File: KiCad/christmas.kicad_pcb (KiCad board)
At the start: 2 copper layers, 81.3 x 81.3 mm, 38 parts, among them J1 Conn_01x04, J2 Conn_01x04, J3 Batery_9V, U1 NE555P, U2 4015, U3 NE555P

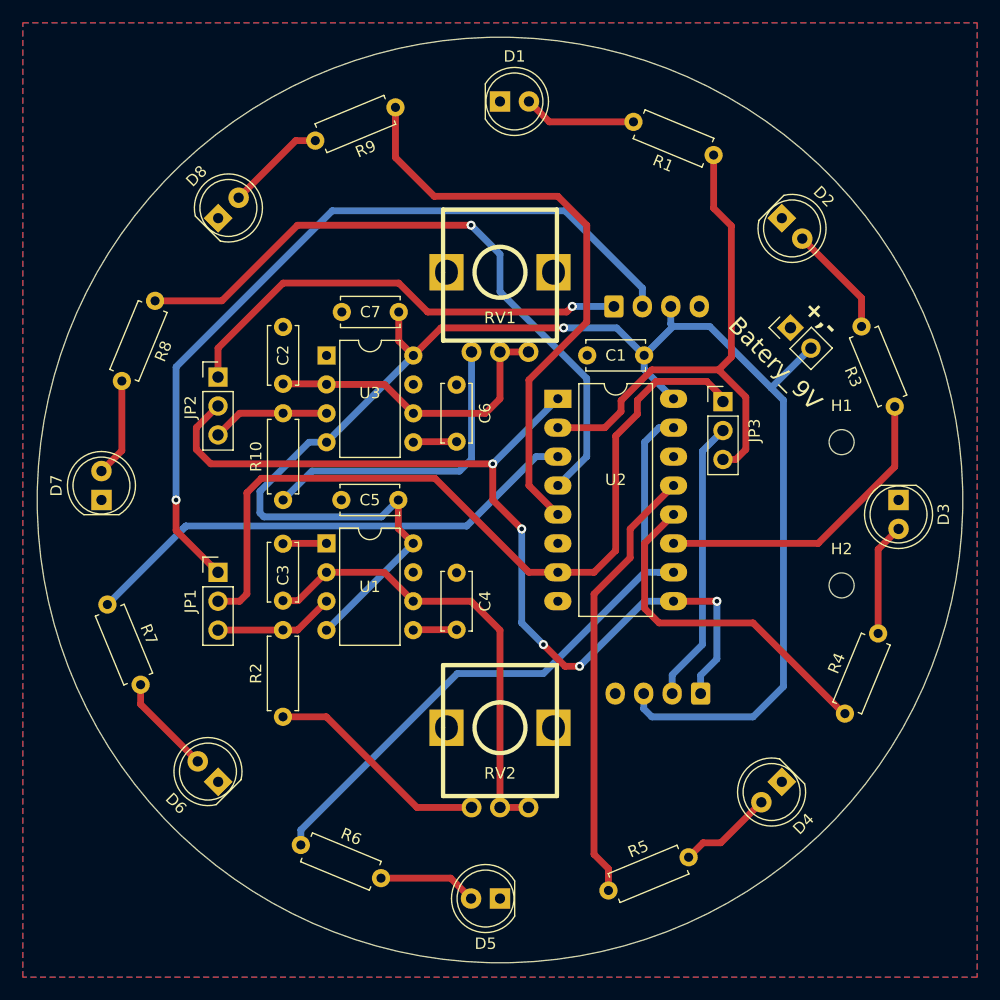
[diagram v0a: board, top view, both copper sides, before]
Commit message: add fablab and vde logos, add rubber band battery holder cutouts
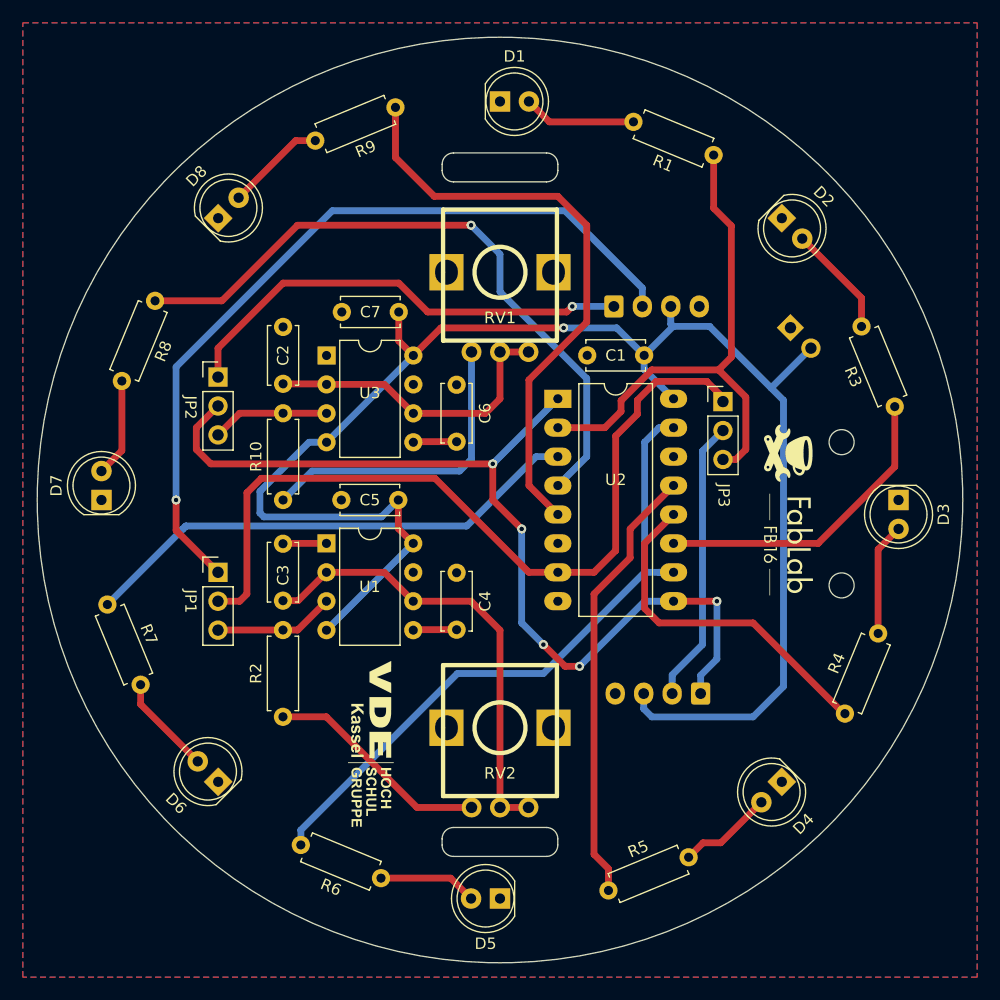
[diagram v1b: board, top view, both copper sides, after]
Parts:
- added G***: LOGO, Logos:vde_hsg_logo, F.Cu at (141.1, 123.1)
- added G***: LOGO, Logos:fablab_logo, F.Cu at (177.7, 102.5)
- J3: value Batery_9V -> Battery_9V; moved to B.Cu
- turned J3 to -135 degrees
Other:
- outline, holes or cut-outs redrawn

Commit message: rewire board2board connector to match "same direction" cables
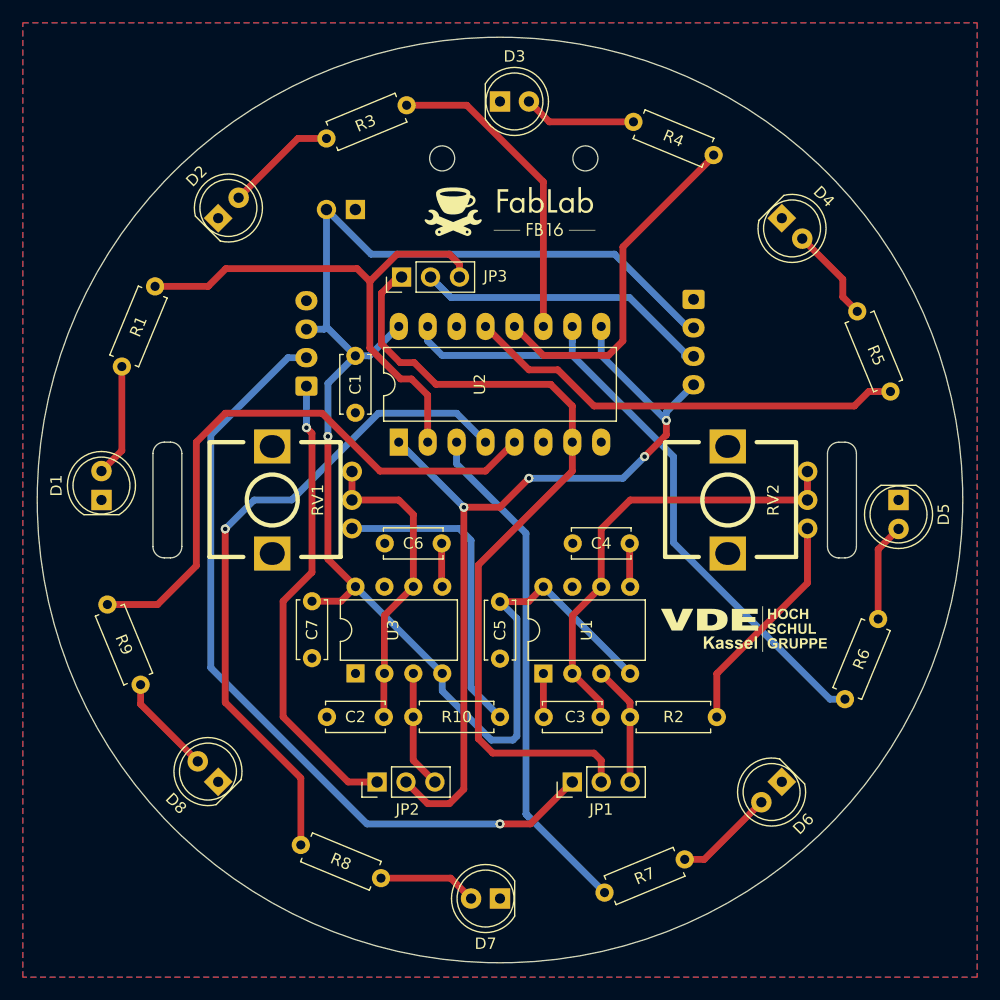
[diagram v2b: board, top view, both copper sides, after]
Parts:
- moved R7 50.5 mm to (161.6, 136.1), turned to 22.5 degrees
- moved R9 50.5 mm to (117.9, 110.8), turned to -67.5 degrees
- moved R4 50.4 mm to (171.2, 71.3), turned to 157.5 degrees
- moved R1 50.4 mm to (122.1, 82.8), turned to -112.5 degrees
- moved R3 50.4 mm to (144.2, 66.9), turned to -157.5 degrees
- moved R5 50.3 mm to (186.7, 92.1), turned to 112.5 degrees
- moved D8 49.5 mm to (127.7, 126.3), turned to 135 degrees
- moved D2 49.5 mm to (127.7, 76.9), turned to 45 degrees
- moved D6 49.5 mm to (177.1, 126.3), turned to -135 degrees
- moved D1 49.5 mm to (117.4, 101.6), turned to 90 degrees
- moved D3 49.5 mm to (152.4, 66.6), turned to 0 degrees
- moved D5 49.5 mm to (187.4, 101.6), turned to -90 degrees
- moved D7 49.5 mm to (152.4, 136.6), turned to 180 degrees
- moved D4 49.5 mm to (177.1, 76.9), turned to -45 degrees
- moved R6 49.5 mm to (182.7, 119.1), turned to 67.5 degrees
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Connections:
- J2 pad 1: Net-(J2-Pin_1) -> GND
- J2 pad 2: Net-(J2-Pin_2) -> VCC
- J2 pad 3: VCC -> Net-(J2-Pin_3)
- J2 pad 4: GND -> Net-(J2-Pin_4)
- JP2 pad 2: Net-(J2-Pin_1) -> Net-(J2-Pin_4)
- JP3 pad 2: Net-(J2-Pin_2) -> Net-(J2-Pin_3)
- U2 pad 1: Net-(J2-Pin_1) -> Net-(J2-Pin_4)
- U2 pad 9: Net-(J2-Pin_1) -> Net-(J2-Pin_4)
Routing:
- net Net-(J2-Pin_1): track 84.1 -> 0.00 mm, vias 5 -> 0
- net Net-(J2-Pin_4): track 0.00 -> 75.7 mm, vias 0 -> 4
- net Net-(J2-Pin_3): track 0.00 -> 25.4 mm
- net Net-(J2-Pin_2): track 24.9 -> 0.00 mm
- net VCC: track 142.8 -> 132.1 mm
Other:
- outline, holes or cut-outs redrawn

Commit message: restructure components on board and implement ToDos from prototyping
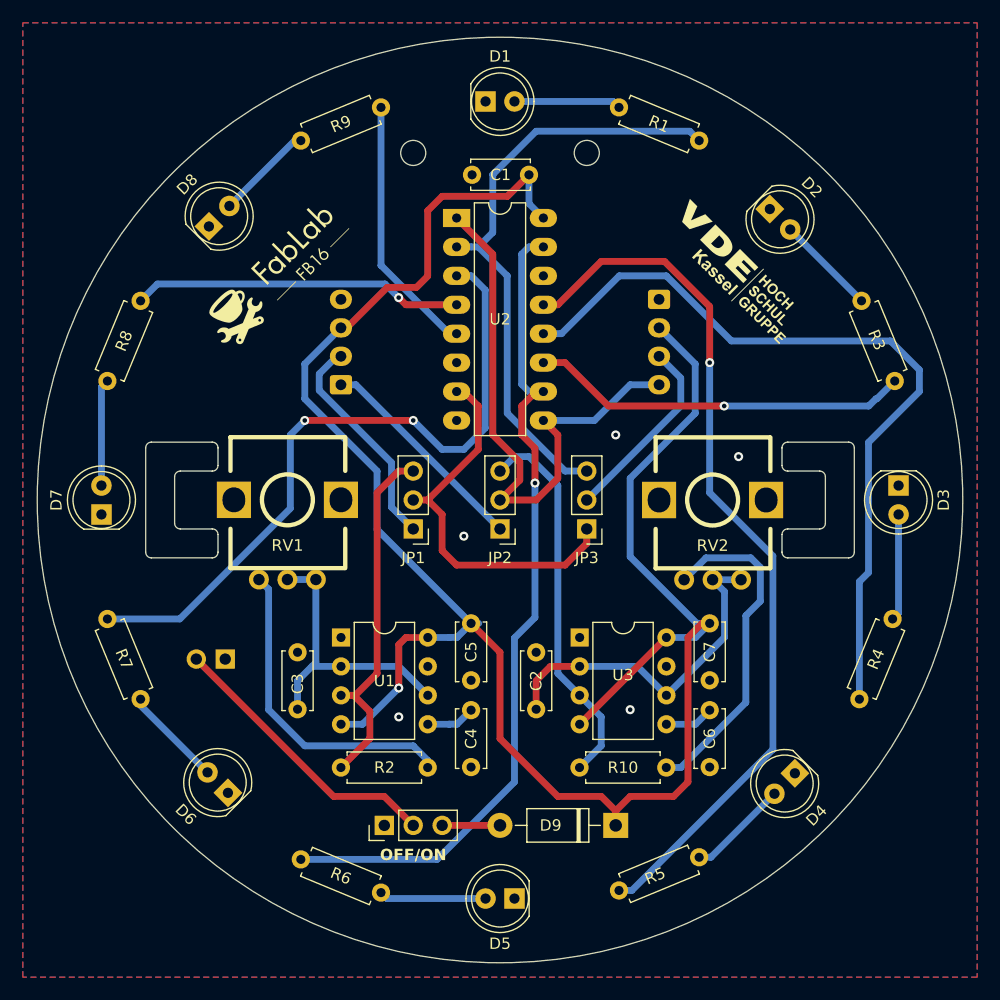
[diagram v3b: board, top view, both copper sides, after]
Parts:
- added D9: 1N5817, Diode_THT:D_DO-41_SOD81_P10.16mm_Horizontal, F.Cu at (162.6, 130.2)
- added ON/OFF1: Jumper_3_Open, Connector_PinHeader_2.54mm:PinHeader_1x03_P2.54mm_Vertical, F.Cu at (142.2, 130.2)
- J2: footprint Connector_JST:JST_XH_S4B-XH-A-1_1x04_P2.50mm_Horizontal -> Connector_JST:JST_XH_S4B-XH-A_1x04_P2.50mm_Horizontal
- U2: footprint Package_DIP:DIP-16_W10.16mm_LongPads -> Package_DIP:DIP-16_W7.62mm_LongPads
- moved R5 49.9 mm to (162.9, 135.9), turned to 22.5 degrees
- moved R7 49.8 mm to (117.9, 112.1), turned to -67.5 degrees
- moved R9 49.8 mm to (141.9, 67.1), turned to -157.5 degrees
- moved R6 49.8 mm to (134.9, 133.2), turned to -22.5 degrees
- moved R8 49.8 mm to (120.8, 84.1), turned to -112.5 degrees
- moved R1 49.5 mm to (169.9, 70.0), turned to 157.5 degrees
- moved R4 49.5 mm to (184.0, 119.1), turned to 67.5 degrees
- moved R3 49.2 mm to (187.1, 91.1), turned to 112.5 degrees
- moved D8 48.8 mm to (126.8, 77.6), turned to 45 degrees
- moved D4 48.8 mm to (178.3, 125.6), turned to -135 degrees
- moved D6 48.6 mm to (128.5, 127.3), turned to 135 degrees
- moved D5 48.6 mm to (153.7, 136.6), turned to 180 degrees
- moved D3 48.6 mm to (187.4, 100.3), turned to -90 degrees
- moved D1 48.6 mm to (151.1, 66.6), turned to 0 degrees
- moved D7 48.6 mm to (117.4, 102.9), turned to 90 degrees
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- renumbered RV2 to RV1, RV1 to RV2
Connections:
- J3 pad 2: VCC -> Net-(J3-Pin_2)
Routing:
- net /Data: track 70.6 -> 19.6 mm, vias 1 -> 0
- net VCC: track 132.1 -> 177.1 mm
- net Net-(U2B-Q2): track 30.7 -> 69.6 mm
- net Net-(U2B-Q1): track 39.0 -> 77.7 mm, vias 0 -> 1
- net Net-(JP1-C): track 72.0 -> 34.1 mm
- net Net-(U2A-Q2): track 58.6 -> 29.1 mm
- net Net-(U2A-Q1): track 52.2 -> 23.0 mm
- net Net-(J3-Pin_2): track 0.00 -> 25.1 mm
- net Net-(J2-Pin_4): track 75.7 -> 50.7 mm, vias 4 -> 0
- net /Timer1/Out: track 10.3 -> 33.8 mm
- net /Timer/Out: track 10.6 -> 32.9 mm
- net /Clk: track 40.9 -> 19.2 mm, vias 1 -> 0
- net Net-(U2A-Q4): track 57.9 -> 74.0 mm, vias 0 -> 1
- net Net-(U2A-Q3): track 45.4 -> 61.2 mm, vias 0 -> 2
- net Net-(U1-THR): track 40.3 -> 25.8 mm
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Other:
- outline, holes or cut-outs redrawn
- board text added: "IN"
- board text added: "J1: Data: Own Timer / IN J2: Clock: Own Timer / IN J3: Push OUT: Data Timer / Shiftregister out"
- board text added: "OFF/ON"
- board text added: "OUT"

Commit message: Added frequency label on front silkscreen for poti
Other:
- board text added: "Freq."
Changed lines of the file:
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@@
     (effects (font (size 1 1) (thickness 0.2) bold) (justify bottom))
+  )
+  (gr_text "Freq." (at 177.038 113.03) (layer "F.SilkS")
+    (effects (font (size 2 2.2) (thickness 0.5) bold) (justify bottom))
   )
   (via (at 162.56 95.885) (size 0.8) (drill 0.4) (layers "F.Cu" "B.Cu") (free) (net 1))
